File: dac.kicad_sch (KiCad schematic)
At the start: 3 parts, among them U3 AD8676xR, U4 AD5791xRUZ, U5 BUF634AxD

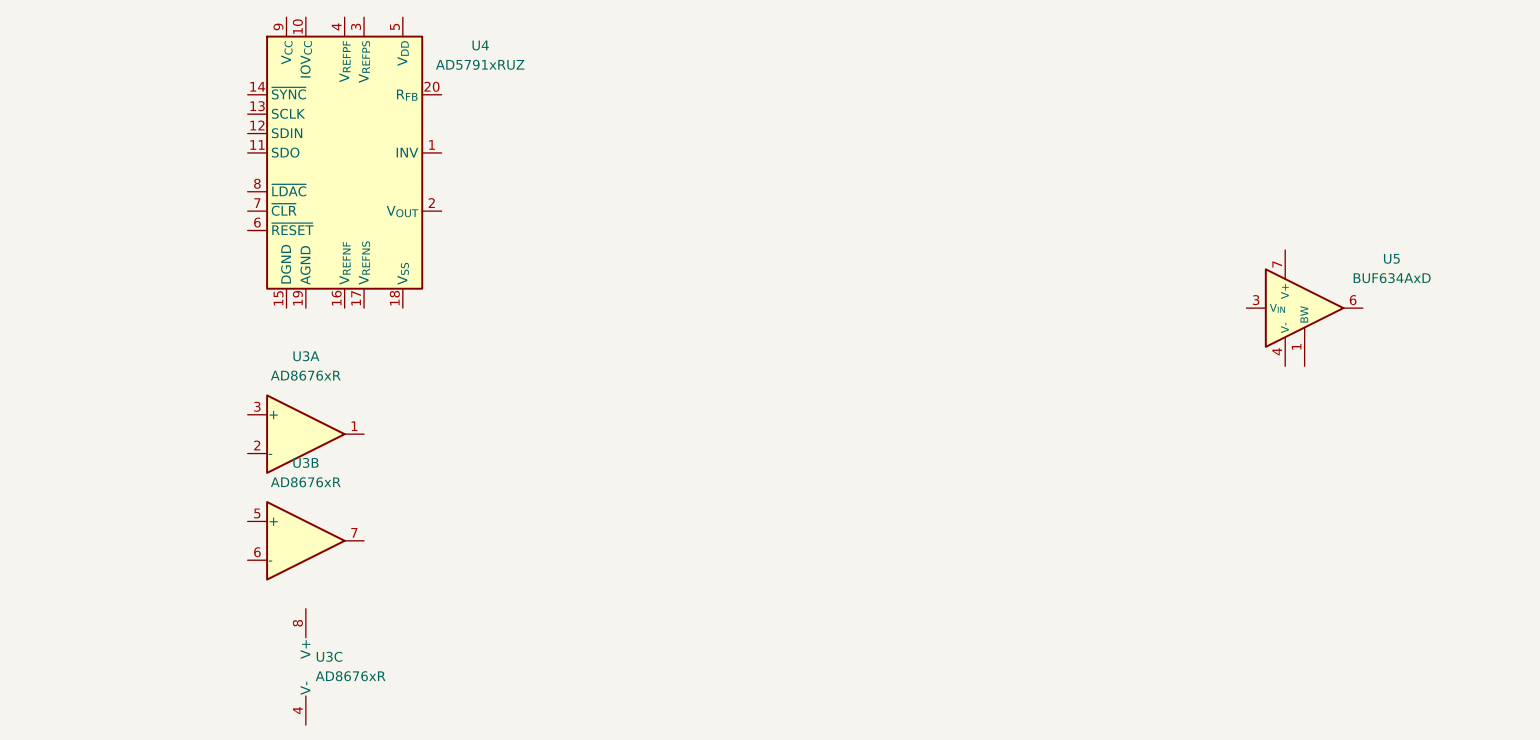
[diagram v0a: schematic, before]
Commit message: Add DAC Sheet
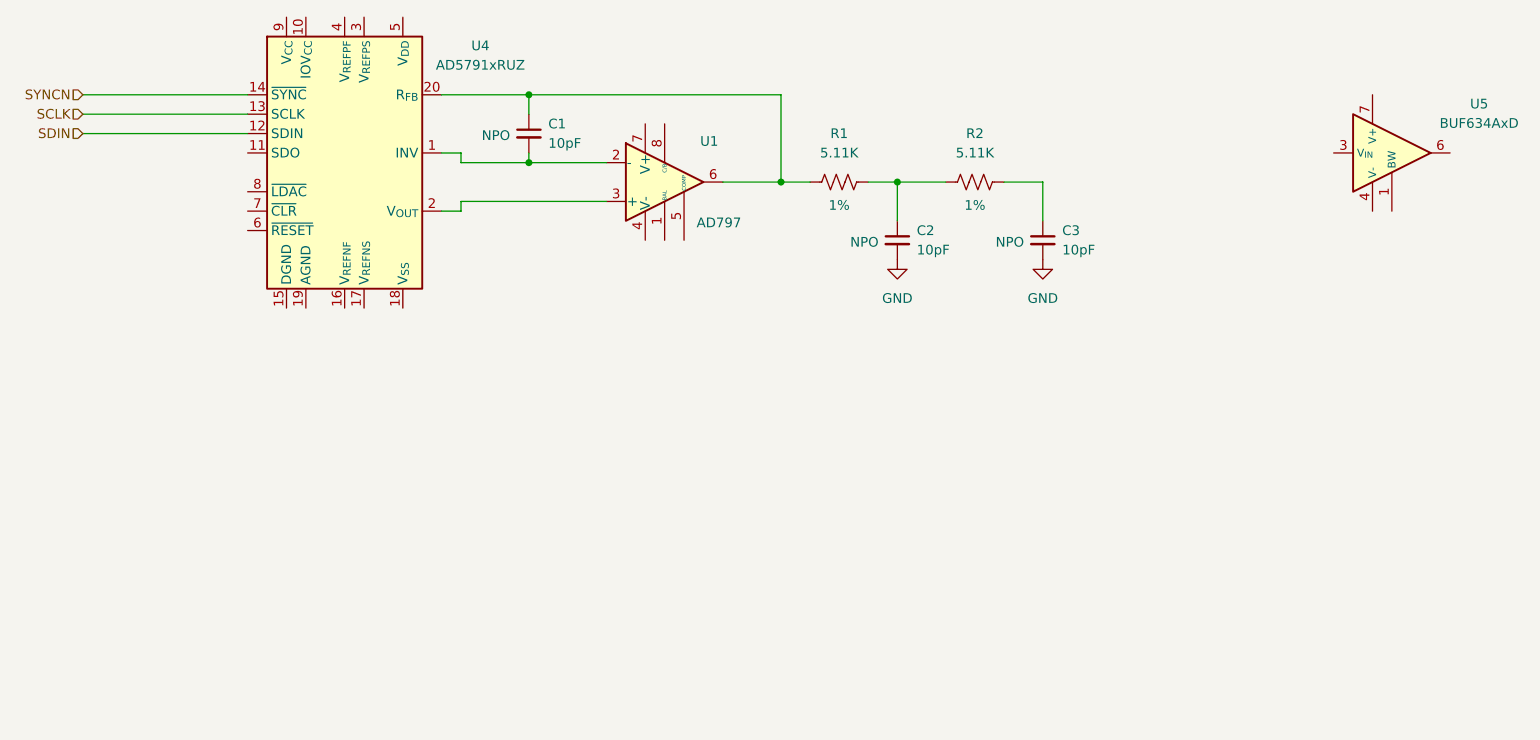
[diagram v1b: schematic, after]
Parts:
- removed U3: AD8676xR, Package_SO:SOIC-8_3.9x4.9mm_P1.27mm, symbol Amplifier_Operational:AD8676xR
- added C1, C2, C3: 10pF, Capacitor_SMD:C_0402_1005Metric, symbol Device:C_Small
- added R1, R2: 5.11K, symbol Device:R_US
- added U1: AD797, Package_SO:SOIC-8_3.9x4.9mm_P1.27mm, symbol PSC:AD797
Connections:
- net at U4.1 (INV): now also C1.2, U1.2 (-)
- net SDIN: now reaches U4.12 (SDIN)
- net SCLK: now reaches U4.13 (SCLK)
- net SYNCN: now reaches U4.14 (~{SYNC})
- net at U4.2 (V_{OUT}): now also U1.3 (+)
- net at U4.20 (R_{FB}): now also C1.1, R1.1, U1.6
- new net: C2.1, R1.2, R2.1
- new net: C3.1, R2.2
- new net GND: C2.2, C3.2
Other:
- moved on the sheet: U5

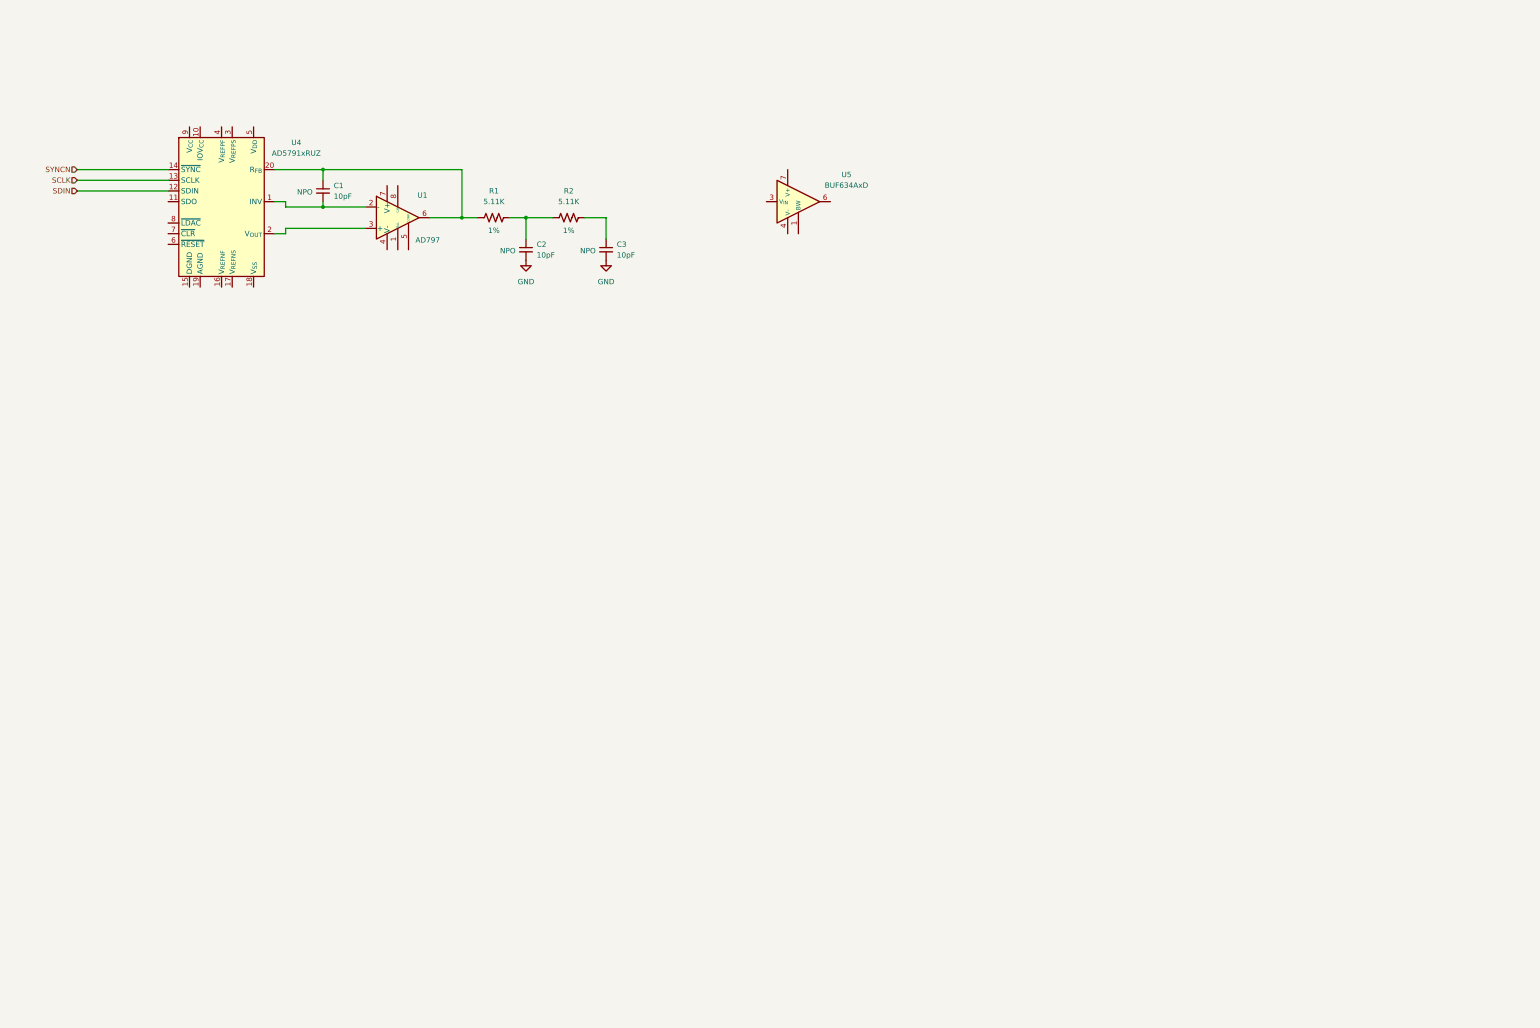
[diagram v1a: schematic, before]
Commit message: DAC section schematic updates
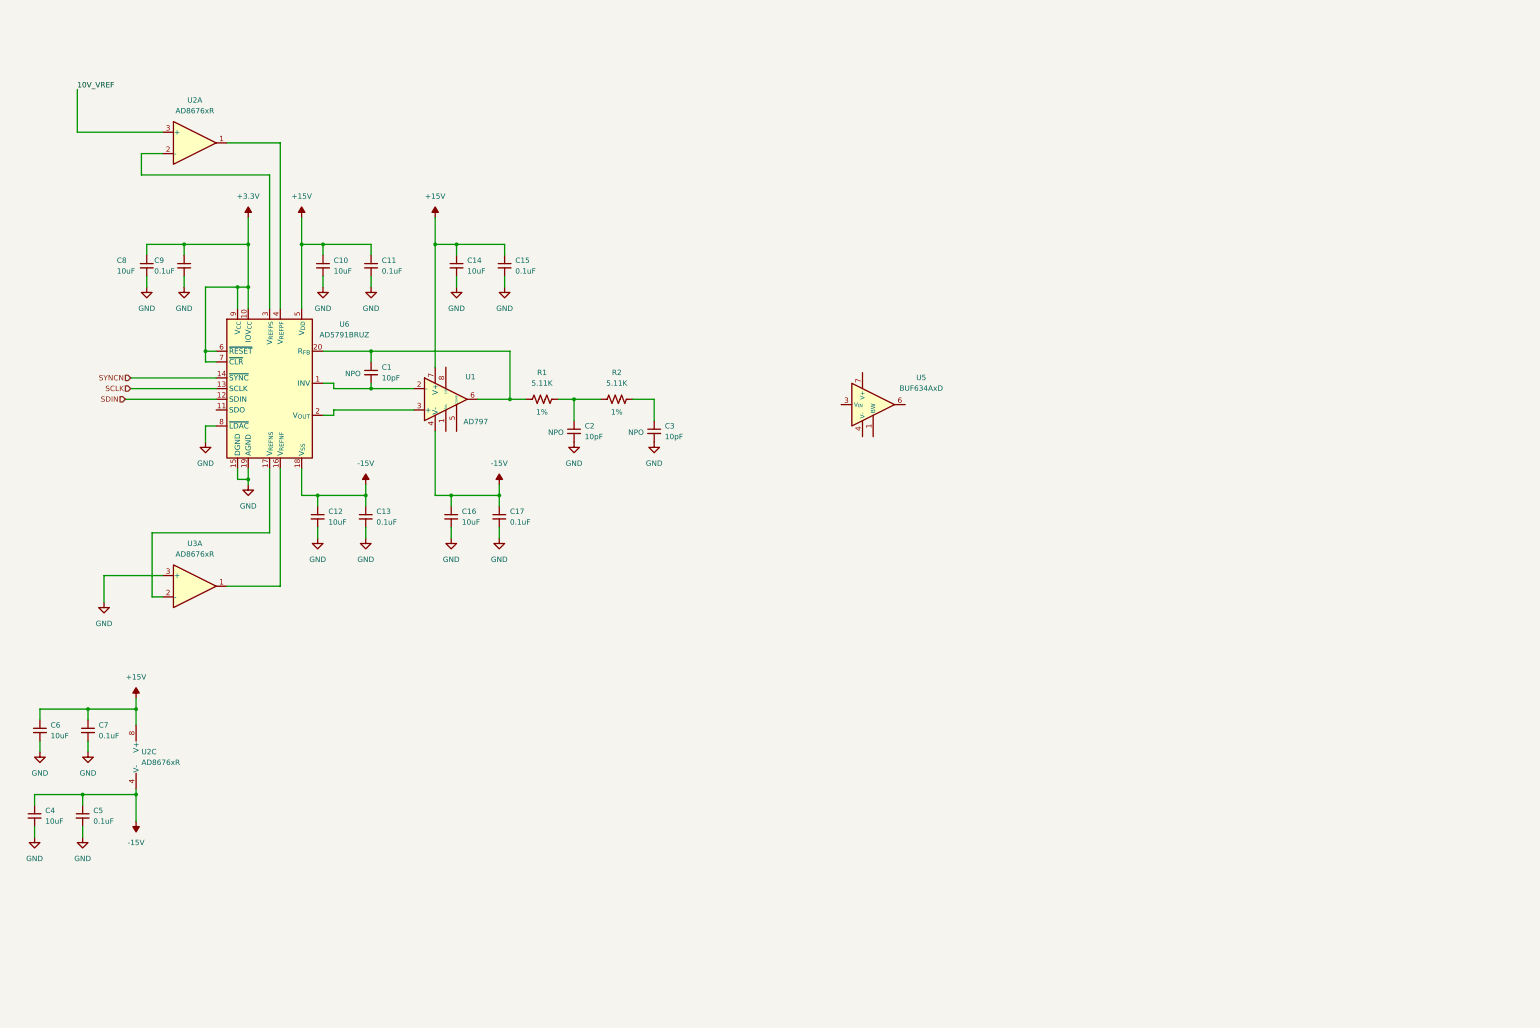
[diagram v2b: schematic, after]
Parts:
- removed U4: AD5791xRUZ, Package_SO:TSSOP-20_4.4x6.5mm_P0.65mm, symbol Analog_DAC:AD5791xRUZ
- added C10, C12, C14, C16, C4, C6, C8: 10uF, Capacitor_SMD:C_0603_1608Metric, symbol Device:C_Small
- added C11, C13, C15, C17, C5, C7, C9: 0.1uF, Capacitor_SMD:C_0402_1005Metric, symbol Device:C_Small
- added U2, U3: AD8676xR, Package_SO:SOIC-8_3.9x4.9mm_P1.27mm, symbol Amplifier_Operational:AD8676xR
- added U6: AD5791BRUZ, Package_SO:TSSOP-20_4.4x6.5mm_P0.65mm, symbol PSC:AD5791BRUZ
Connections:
- net GND: now also C10.2, C11.2, C12.2, C13.2, C14.2, C15.2, C16.2, C17.2, C4.2, C5.2, C6.2, C7.2, C8.2, C9.2, U3.3 (+), U6.15 (DGND), U6.19 (AGND), U6.8 (~{LDAC})
- net SCLK: now also U6.13 (SCLK)
- net SDIN: now also U6.12 (SDIN)
- net SYNCN: now also U6.14 (~{SYNC})
- net at C1.1, R1.1, U1.6: now also U6.20 (R_{FB})
- net at C1.2, U1.2 (-): now also U6.1 (INV)
- net at U1.3 (+): now also U6.2 (V_{OUT})
- net -15V: now reaches U1.4 (V-)
- net -15V: now also C12.1, C13.1, C16.1, C17.1, C4.1, C5.1, U2.4 (V-), U6.18 (V_{SS})
- net +15V: now reaches U1.7 (V+)
- net +15V: now also C10.1, C11.1, C14.1, C15.1, C6.1, C7.1, U2.8 (V+), U6.5 (V_{DD})
- new net: U3.1, U6.16 (V_{REFNF})
- new net: U3.2 (-), U6.17 (V_{REFNS})
- new net: U2.2 (-), U6.3 (V_{REFPS})
- new net: U2.1, U6.4 (V_{REFPF})
- new net +3.3V: C8.1, C9.1, U6.10 (IOV_{CC}), U6.6 (~{RESET}), U6.7 (~{CLR}), U6.9 (V_{CC})
- new net 10V_VREF: U2.3 (+)
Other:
- moved on the sheet: C1, C2, C3, R1, R2, U1, U5

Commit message: Add ADR1001 Voltage Reference
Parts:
- added C18, C20, C22, C23, C26, C27, C30, C31, C34, C35: 10uF, Capacitor_SMD:C_0603_1608Metric, symbol Device:C_Small
- added C19, C21, C24, C25, C28, C29, C32, C33, C36, C37: 0.1uF, Capacitor_SMD:C_0402_1005Metric, symbol Device:C_Small
- added R3, R4: 100, Resistor_SMD:R_0603_1608Metric, symbol Device:R_US
- added U4, U7, U9: OPA277, Package_SO:SOIC-8_3.9x4.9mm_P1.27mm, symbol PSC:opa277
- added U8: BUF634AxD, Package_SO:SOIC-8_3.9x4.9mm_P1.27mm, symbol Amplifier_Buffer:BUF634AxD
- R1, R2: footprint (none) -> Resistor_SMD:R_0402_1005Metric
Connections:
- net +15V: now also U5.7 (V+), C18.1, C19.1, C23.1, C25.1, C27.1, C29.1, C31.1, C33.1, C35.1, C37.1, U4.7 (V+), U7.7 (V+), U8.7 (V+), U9.7 (V+)
- net -15V: now also U5.4 (V-), C20.1, C21.1, C22.1, C24.1, C26.1, C28.1, C30.1, C32.1, C34.1, C36.1, U4.4 (V-), U7.4 (V-), U8.4 (V-), U9.4 (V-)
- net 10V_VREF: no longer U2.3 (+)
- net GND: now also C18.2, C19.2, C20.2, C21.2, C22.2, C23.2, C24.2, C25.2, C26.2, C27.2, C28.2, C29.2, C30.2, C31.2, C32.2, C33.2, C34.2, C35.2, C36.2, C37.2, U4.3 (+), U9.3 (+)
- net dac_mon: now reaches C3.1, R2.2
- net dac_mon: now also U4.2 (-), U4.6, U7.3 (+)
- net at U5.3 (V_{IN}): now also U7.6
- net at U5.6: now also R3.1, U7.2 (-)
- new net: R4.1, U8.6, U9.2 (-)
- new net: U8.3 (V_{IN}), U9.6
- new net Voltage Reference/REF_OUT: U2.3 (+)
- new net control_vout+: R3.2
- new net control_vout-: R4.2
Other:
- added sheet Voltage Reference (volt_ref.kicad_sch)
- note added: "Low Pass Filter"
- note added: "Output Driver"
- moved on the sheet: C1, C10, C11, C12, C13, C14, C15, C16, C17, C2, C3, C4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

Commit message: Add isolated digital I/O
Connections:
- net SCLK renamed sclk
- net SDIN renamed sdin
- net SYNCN renamed syncn
- net control_vout+ renamed dac_out+
- net control_vout- renamed dac_vout-
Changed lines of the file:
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@@
 	(wire
 		(pts
-			(xy 60.96 115.57) (xy 82.55 115.57)
+			(xy 62.23 115.57) (xy 82.55 115.57)
 		)
 		(stroke
@@
 		)
 	)
-	(hierarchical_label "SCLK"
+	(hierarchical_label "sclk"
 		(shape input)
 		(at 62.23 113.03 180)
@@
 		)
 	)
-	(hierarchical_label "SYNCN"
+	(hierarchical_label "syncn"
 		(shape input)
 		(at 62.23 110.49 180)
@@
 		)
 	)
-	(hierarchical_label "SDIN"
-		(shape input)
-		(at 60.96 115.57 180)
+	(hierarchical_label "sdin"
+		(shape input)
+		(at 62.23 115.57 180)
 		(effects
 			(font
@@
 		)
 	)
-	(hierarchical_label "control_vout+"
+	(hierarchical_label "dac_out+"
 		(shape input)
 		(at 363.22 167.64 0)
@@
 		)
 	)
-	(hierarchical_label "control_vout-"
+	(hierarchical_label "dac_vout-"
 		(shape input)
 		(at 363.22 177.8 0)

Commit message: Add DCCT ADCs
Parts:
- renumbered C4 to C11, C6 to C12, C5 to C13, C7 to C14, C8 to C15, C9 to C16, C12 to C17, C10 to C18, C13 to C19, C11 to C20, C1 to C21, C16 to C22, C14 to C23, C17 to C24, C15 to C25, C2 to C26, C3 to C27, C26 to C28, C34 to C29, C20 to C30, C27 to C31, C35 to C32, C18 to C33, C28 to C34, C36 to C35, C21 to C36, C29 to C37, C37 to C38, C19 to C39, C30 to C40, C22 to C41, C31 to C42, C23 to C43, C32 to C44, C24 to C45, C33 to C46, C25 to C47, R4 to R10, R1 to R7, R2 to R8, R3 to R9, U8 to U10, U5 to U11, U2 to U3, U3 to U4, U6 to U5, U1 to U6, U9 to U7, U4 to U8, U7 to U9

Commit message: finish rough placement
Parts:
- removed C29, C32: 10uF, Capacitor_SMD:C_0603_1608Metric, symbol Device:C_Small
- removed C35, C38: 0.1uF, Capacitor_SMD:C_0402_1005Metric, symbol Device:C_Small
- removed U4: AD8676xR, Package_SO:SOIC-8_3.9x4.9mm_P1.27mm, symbol Amplifier_Operational:AD8676xR
- removed U8: OPA277, Package_SO:SOIC-8_3.9x4.9mm_P1.27mm, symbol PSC:opa277
- added unit 2 of U3
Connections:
- net GND: now also U3.5 (+)
- net at U5.16 (V_{REFNF}): now also U3.7
- net at U5.17 (V_{REFNS}): now also U3.6 (-)

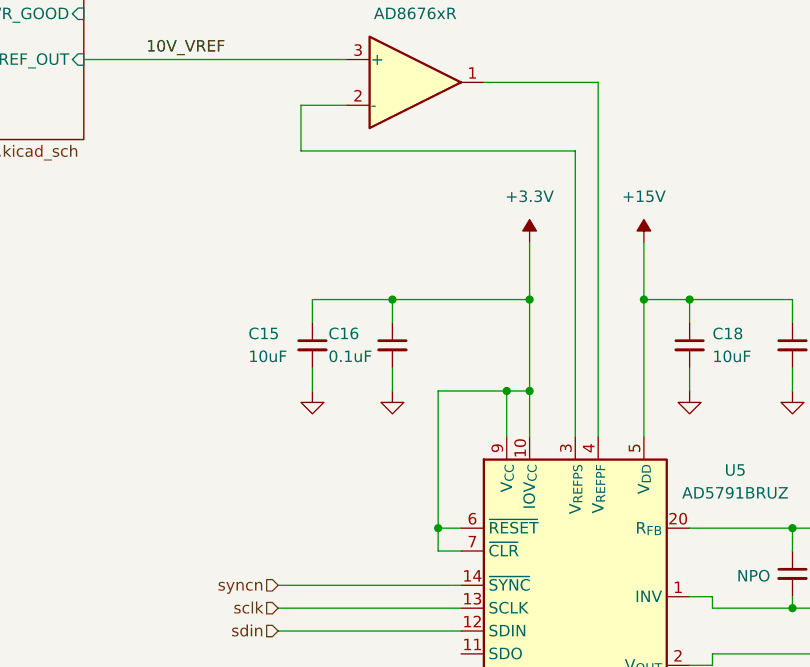
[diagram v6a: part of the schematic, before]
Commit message: Change DAC outputs to 1.8v
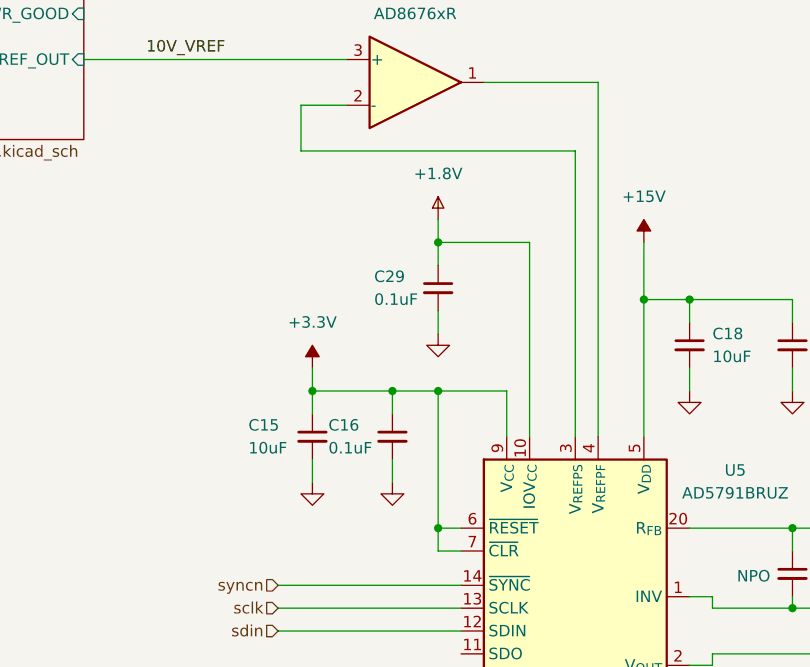
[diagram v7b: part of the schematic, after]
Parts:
- added C29: 0.1uF, Capacitor_SMD:C_0402_1005Metric, symbol Device:C_Small
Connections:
- net +3.3V: no longer U5.10 (IOV_{CC})
- net GND: now also C29.2
- new net +1.8V: C29.1, U5.10 (IOV_{CC})
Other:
- moved on the sheet: C15, C16

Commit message: Finish layout
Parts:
- added D1: DFLS130-7, myparts:DFLS130-7_DIO, symbol PSC:DFLS130-7
- C11, C12, C15, C17, C18, C22, C23, C28, C30, C31, C33, C40, C41, C42, C43: MFG (none) -> Samsung; MFG_PN (none) -> CL10A106MA8NRNC
- C13, C14, C16, C19, C20, C24, C25, C29, C34, C36, C37, C39, C44, C45, C46, C47: MFG (none) -> Taiyo Yuden; MFG_PN (none) -> TMK105BJ104KV-F
- C21, C26, C27: MFG (none) -> Kemet; MFG_PN (none) -> C0402C100K5RACTU
- R10, R9: Cost (none) -> .01; MFG (none) -> Panasonic; MFG_PN (none) -> ERJ-2RKF15R0X
- R7, R8: Cost (none) -> .01; MFG (none) -> Panasonic; MFG_PN (none) -> ERJ-2RKF5111X
- U10, U11: value BUF634AxD -> BUF634AIDR; Cost (none) -> 2.99; MFG (none) -> Analog Devices; MFG_PN (none) -> BUF634AIDR
- U3: value AD8676xR -> AD8676ARZ; Cost (none) -> 3.93; MFG (none) -> Analog Devices; MFG_PN (none) -> AD8676ARZ-REEL7
- U5: Cost (none) -> 129.29; MFG (none) -> Analog Devices; MFG_PN (none) -> AD5791BRUZ
- U6: value AD797 -> AD797ARZ; Cost (none) -> 13.75; MFG (none) -> Analog Devices; MFG_PN (none) -> AD797ARZ
- U7, U9: Cost (none) -> 2.66; MFG (none) -> Analog Devices; MFG_PN (none) -> OPA277UA/2K5
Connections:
- net +15V: now also D1.1 (K)
- net +3.3V: now also D1.2 (A)
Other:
- moved on the sheet: U3A
